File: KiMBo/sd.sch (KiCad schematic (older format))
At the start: 9 parts

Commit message: Annotate all components, now passing ERC, added ferrites to the rest of the connectors
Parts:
- gave numbers to parts that had none: 9
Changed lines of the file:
@@
 $Descr A4 11693 8268
 encoding utf-8
-Sheet 10 26
+Sheet 13 26
 Title ""
 Date ""
@@
 $EndDescr
 $Comp
-L CP1 C?
+L CP1 C65
 U 1 1 589C8DA1
 P 6900 2750
-F 0 "C?" H 7015 2796 50  0000 L CNN
+F 0 "C65" H 7015 2796 50  0000 L CNN
 F 1 "CP1" H 7015 2705 50  0000 L CNN
 F 2 "" H 6900 2750 50  0000 C CNN
@@
 $EndComp
 $Comp
-L CP1 C?
+L CP1 C66
 U 1 1 589C8DE9
 P 7100 2750
-F 0 "C?" H 7215 2796 50  0000 L CNN
+F 0 "C66" H 7215 2796 50  0000 L CNN
 F 1 "CP1" H 7215 2705 50  0000 L CNN
 F 2 "" H 7100 2750 50  0000 C CNN
@@
 Connection ~ 7000 2950
 $Comp
-L GND #PWR0166
+L GND #PWR0146
 U 1 1 589C8FE8
 P 7000 3000
-F 0 "#PWR0166" H 7000 2750 50  0001 C CNN
+F 0 "#PWR0146" H 7000 2750 50  0001 C CNN
 F 1 "GND" H 7005 2827 50  0000 C CNN
 F 2 "" H 7000 3000 50  0000 C CNN
@@
 	4800 3900 6600 3900
 $Comp
-L R R?
+L R R99
 U 1 1 58F3951D
 P 5300 3100
-F 0 "R?" H 5370 3146 50  0000 L CNN
+F 0 "R99" H 5370 3146 50  0000 L CNN
 F 1 "R" H 5370 3055 50  0000 L CNN
 F 2 "" V 5230 3100 50  0000 C CNN
@@
 $EndComp
 $Comp
-L R R?
+L R R100
 U 1 1 58F3959D
 P 5550 3100
-F 0 "R?" H 5620 3146 50  0000 L CNN
+F 0 "R100" H 5620 3146 50  0000 L CNN
 F 1 "R" H 5620 3055 50  0000 L CNN
 F 2 "" V 5480 3100 50  0000 C CNN
@@
 $EndComp
 $Comp
-L R R?
+L R R101
 U 1 1 58F395D9
 P 5800 3100
-F 0 "R?" H 5870 3146 50  0000 L CNN
+F 0 "R101" H 5870 3146 50  0000 L CNN
 F 1 "R" H 5870 3055 50  0000 L CNN
 F 2 "" V 5730 3100 50  0000 C CNN
@@
 $EndComp
 $Comp
-L R R?
+L R R102
 U 1 1 58F39A19
 P 6050 3100
-F 0 "R?" H 6120 3146 50  0000 L CNN
+F 0 "R102" H 6120 3146 50  0000 L CNN
 F 1 "R" H 6120 3055 50  0000 L CNN
 F 2 "" V 5980 3100 50  0000 C CNN
@@
 $EndComp
 $Comp
-L R R?
+L R R103
 U 1 1 58F39B2F
 P 6300 3100
-F 0 "R?" H 6370 3146 50  0000 L CNN
+F 0 "R103" H 6370 3146 50  0000 L CNN
 F 1 "R" H 6370 3055 50  0000 L CNN
 F 2 "" V 6230 3100 50  0000 C CNN
@@
 $EndComp
 $Comp
-L R R?
+L R R104
 U 1 1 58F39B72
 P 6550 3100
-F 0 "R?" H 6620 3146 50  0000 L CNN
+F 0 "R104" H 6620 3146 50  0000 L CNN
 F 1 "R" H 6620 3055 50  0000 L CNN
 F 2 "" V 6480 3100 50  0000 C CNN
@@
 SPI0_CS1
 $Comp
-L R R?
+L R R98
 U 1 1 58F3C883
 P 5050 3100
-F 0 "R?" H 5120 3146 50  0000 L CNN
+F 0 "R98" H 5120 3146 50  0000 L CNN
 F 1 "R" H 5120 3055 50  0000 L CNN
 F 2 "" V 4980 3100 50  0000 C CNN
@@
 G17
 $Comp
-L VDD_3V3B #PWR0167
+L VDD_3V3B #PWR0147
 U 1 1 5A066650
 P 5800 2850
-F 0 "#PWR0167" H 5800 2700 50  0001 C CNN
+F 0 "#PWR0147" H 5800 2700 50  0001 C CNN
 F 1 "VDD_3V3B" H 5815 3023 50  0000 C CNN
 F 2 "" H 5800 2850 50  0000 C CNN
@@
 $EndComp
 $Comp
-L VDD_3V3B #PWR0168
+L VDD_3V3B #PWR0148
 U 1 1 5A066680
 P 7000 2500
-F 0 "#PWR0168" H 7000 2350 50  0001 C CNN
+F 0 "#PWR0148" H 7000 2350 50  0001 C CNN
 F 1 "VDD_3V3B" H 7015 2673 50  0000 C CNN
 F 2 "" H 7000 2500 50  0000 C CNN

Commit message: Clean up various parts of the schematic, high level sheet has annoated modules
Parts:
- renumbered C65 to C42, C66 to C43, R98 to R86, R99 to R87, R100 to R88, R101 to R89, R102 to R90, R103 to R91, R104 to R92
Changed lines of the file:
@@
 $Descr A4 11693 8268
 encoding utf-8
-Sheet 13 26
+Sheet 9 26
 Title ""
 Date ""
@@
 $EndDescr
 $Comp
-L CP1 C65
+L CP1 C42
 U 1 1 589C8DA1
 P 6900 2750
-F 0 "C65" H 7015 2796 50  0000 L CNN
+F 0 "C42" H 7015 2796 50  0000 L CNN
 F 1 "CP1" H 7015 2705 50  0000 L CNN
 F 2 "" H 6900 2750 50  0000 C CNN
@@
 $EndComp
 $Comp
-L CP1 C66
+L CP1 C43
 U 1 1 589C8DE9
 P 7100 2750
-F 0 "C66" H 7215 2796 50  0000 L CNN
+F 0 "C43" H 7215 2796 50  0000 L CNN
 F 1 "CP1" H 7215 2705 50  0000 L CNN
 F 2 "" H 7100 2750 50  0000 C CNN
@@
 	4800 3900 6600 3900
 $Comp
-L R R99
+L R R87
 U 1 1 58F3951D
 P 5300 3100
-F 0 "R99" H 5370 3146 50  0000 L CNN
+F 0 "R87" H 5370 3146 50  0000 L CNN
 F 1 "R" H 5370 3055 50  0000 L CNN
 F 2 "" V 5230 3100 50  0000 C CNN
@@
 $EndComp
 $Comp
-L R R100
+L R R88
 U 1 1 58F3959D
 P 5550 3100
-F 0 "R100" H 5620 3146 50  0000 L CNN
+F 0 "R88" H 5620 3146 50  0000 L CNN
 F 1 "R" H 5620 3055 50  0000 L CNN
 F 2 "" V 5480 3100 50  0000 C CNN
@@
 $EndComp
 $Comp
-L R R101
+L R R89
 U 1 1 58F395D9
 P 5800 3100
-F 0 "R101" H 5870 3146 50  0000 L CNN
+F 0 "R89" H 5870 3146 50  0000 L CNN
 F 1 "R" H 5870 3055 50  0000 L CNN
 F 2 "" V 5730 3100 50  0000 C CNN
@@
 $EndComp
 $Comp
-L R R102
+L R R90
 U 1 1 58F39A19
 P 6050 3100
-F 0 "R102" H 6120 3146 50  0000 L CNN
+F 0 "R90" H 6120 3146 50  0000 L CNN
 F 1 "R" H 6120 3055 50  0000 L CNN
 F 2 "" V 5980 3100 50  0000 C CNN
@@
 $EndComp
 $Comp
-L R R103
+L R R91
 U 1 1 58F39B2F
 P 6300 3100
-F 0 "R103" H 6370 3146 50  0000 L CNN
+F 0 "R91" H 6370 3146 50  0000 L CNN
 F 1 "R" H 6370 3055 50  0000 L CNN
 F 2 "" V 6230 3100 50  0000 C CNN
@@
 $EndComp
 $Comp
-L R R104
+L R R92
 U 1 1 58F39B72
 P 6550 3100
-F 0 "R104" H 6620 3146 50  0000 L CNN
+F 0 "R92" H 6620 3146 50  0000 L CNN
 F 1 "R" H 6620 3055 50  0000 L CNN
 F 2 "" V 6480 3100 50  0000 C CNN
@@
 SPI0_CS1
 $Comp
-L R R98
+L R R86
 U 1 1 58F3C883
 P 5050 3100
-F 0 "R98" H 5120 3146 50  0000 L CNN
+F 0 "R86" H 5120 3146 50  0000 L CNN
 F 1 "R" H 5120 3055 50  0000 L CNN
 F 2 "" V 4980 3100 50  0000 C CNN

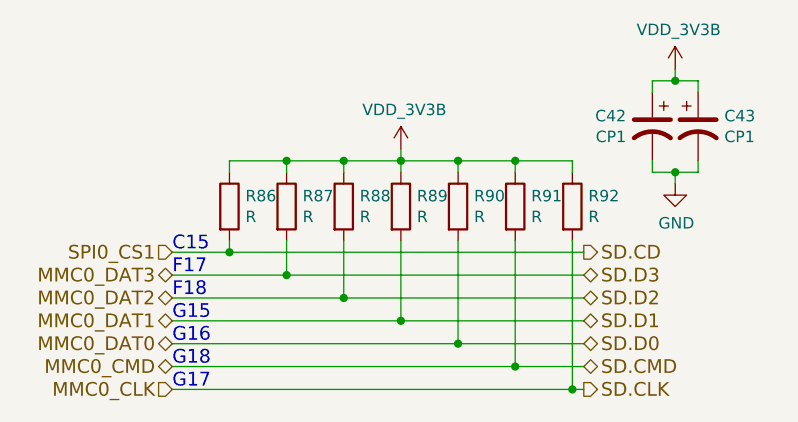
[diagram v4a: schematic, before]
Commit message: Entry of additional component values
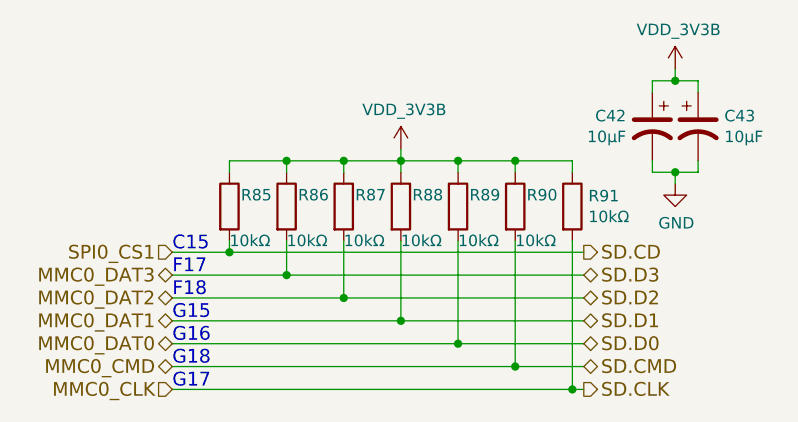
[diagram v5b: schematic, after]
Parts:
- C42, C43: value CP1 -> 10μF
- R85: renamed from R86; value R -> 10kΩ
- R86: renamed from R87; value R -> 10kΩ
- R87: renamed from R88; value R -> 10kΩ
- R88: renamed from R89; value R -> 10kΩ
- R89: renamed from R90; value R -> 10kΩ
- R90: renamed from R91; value R -> 10kΩ
- R91: renamed from R92; value R -> 10kΩ
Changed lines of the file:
@@
 P 6900 2750
 F 0 "C42" H 7015 2796 50  0000 L CNN
-F 1 "CP1" H 7015 2705 50  0000 L CNN
+F 1 "10μF" H 7015 2705 50  0000 L CNN
 F 2 "" H 6900 2750 50  0001 C CNN
 F 3 "" H 6900 2750 50  0000 C CNN
@@
 P 7100 2750
 F 0 "C43" H 7215 2796 50  0000 L CNN
-F 1 "CP1" H 7215 2705 50  0000 L CNN
+F 1 "10μF" H 7215 2705 50  0000 L CNN
 F 2 "" H 7100 2750 50  0001 C CNN
 F 3 "" H 7100 2750 50  0000 C CNN
@@
 Connection ~ 7000 2950
 $Comp
-L GND #PWR0146
+L GND #PWR0147
 U 1 1 589C8FE8
 P 7000 3000
-F 0 "#PWR0146" H 7000 2750 50  0001 C CNN
+F 0 "#PWR0147" H 7000 2750 50  0001 C CNN
 F 1 "GND" H 7005 2827 50  0000 C CNN
 F 2 "" H 7000 3000 50  0000 C CNN
@@
 	4800 3900 6600 3900
 $Comp
-L R R87
+L R R86
 U 1 1 58F3951D
 P 5300 3100
-F 0 "R87" H 5370 3146 50  0000 L CNN
-F 1 "R" H 5370 3055 50  0000 L CNN
+F 0 "R86" H 5350 3150 50  0000 L CNN
+F 1 "10kΩ" H 5300 2950 50  0000 L CNN
 F 2 "" V 5230 3100 50  0001 C CNN
 F 3 "" H 5300 3100 50  0000 C CNN
@@
 $EndComp
 $Comp
-L R R88
+L R R87
 U 1 1 58F3959D
 P 5550 3100
-F 0 "R88" H 5620 3146 50  0000 L CNN
-F 1 "R" H 5620 3055 50  0000 L CNN
+F 0 "R87" H 5600 3150 50  0000 L CNN
+F 1 "10kΩ" H 5550 2950 50  0000 L CNN
 F 2 "" V 5480 3100 50  0001 C CNN
 F 3 "" H 5550 3100 50  0000 C CNN
@@
 $EndComp
 $Comp
-L R R89
+L R R88
 U 1 1 58F395D9
 P 5800 3100
-F 0 "R89" H 5870 3146 50  0000 L CNN
-F 1 "R" H 5870 3055 50  0000 L CNN
+F 0 "R88" H 5850 3150 50  0000 L CNN
+F 1 "10kΩ" H 5800 2950 50  0000 L CNN
 F 2 "" V 5730 3100 50  0001 C CNN
 F 3 "" H 5800 3100 50  0000 C CNN
@@
 $EndComp
 $Comp
-L R R90
+L R R89
 U 1 1 58F39A19
 P 6050 3100
-F 0 "R90" H 6120 3146 50  0000 L CNN
-F 1 "R" H 6120 3055 50  0000 L CNN
+F 0 "R89" H 6100 3150 50  0000 L CNN
+F 1 "10kΩ" H 6050 2950 50  0000 L CNN
 F 2 "" V 5980 3100 50  0001 C CNN
 F 3 "" H 6050 3100 50  0000 C CNN
@@
 $EndComp
 $Comp
-L R R91
+L R R90
 U 1 1 58F39B2F
 P 6300 3100
-F 0 "R91" H 6370 3146 50  0000 L CNN
-F 1 "R" H 6370 3055 50  0000 L CNN
+F 0 "R90" H 6350 3150 50  0000 L CNN
+F 1 "10kΩ" H 6300 2950 50  0000 L CNN
 F 2 "" V 6230 3100 50  0001 C CNN
 F 3 "" H 6300 3100 50  0000 C CNN
@@
 $EndComp
 $Comp
-L R R92
+L R R91
 U 1 1 58F39B72
 P 6550 3100
-F 0 "R92" H 6620 3146 50  0000 L CNN
-F 1 "R" H 6620 3055 50  0000 L CNN
+F 0 "R91" H 6620 3146 50  0000 L CNN
+F 1 "10kΩ" H 6620 3055 50  0000 L CNN
 F 2 "" V 6480 3100 50  0001 C CNN
 F 3 "" H 6550 3100 50  0000 C CNN
@@
 SPI0_CS1
 $Comp
-L R R86
+L R R85
 U 1 1 58F3C883
 P 5050 3100
-F 0 "R86" H 5120 3146 50  0000 L CNN
-F 1 "R" H 5120 3055 50  0000 L CNN
+F 0 "R85" H 5100 3150 50  0000 L CNN
+F 1 "10kΩ" H 5050 2950 50  0000 L CNN
 F 2 "" V 4980 3100 50  0001 C CNN
 F 3 "" H 5050 3100 50  0000 C CNN
@@
 G17
 $Comp
-L VDD_3V3B #PWR0147
+L VDD_3V3B #PWR0148
 U 1 1 5A066650
 P 5800 2850
-F 0 "#PWR0147" H 5800 2700 50  0001 C CNN
+F 0 "#PWR0148" H 5800 2700 50  0001 C CNN
 F 1 "VDD_3V3B" H 5815 3023 50  0000 C CNN
 F 2 "" H 5800 2850 50  0000 C CNN
@@
 $EndComp
 $Comp
-L VDD_3V3B #PWR0148
+L VDD_3V3B #PWR0149
 U 1 1 5A066680
 P 7000 2500
-F 0 "#PWR0148" H 7000 2350 50  0001 C CNN
+F 0 "#PWR0149" H 7000 2350 50  0001 C CNN
 F 1 "VDD_3V3B" H 7015 2673 50  0000 C CNN
 F 2 "" H 7000 2500 50  0000 C CNN

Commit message: Replace most electrolytic cap symbols symbols with the standard, non-polarized (ceramic) cap symbol
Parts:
- C42, C43: symbol CP1 -> C
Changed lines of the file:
@@
 $EndDescr
 $Comp
-L CP1 C42
+L C C42
 U 1 1 589C8DA1
 P 6900 2750
@@
 $EndComp
 $Comp
-L CP1 C43
+L C C43
 U 1 1 589C8DE9
 P 7100 2750

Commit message: Associate more footprints
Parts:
- C42, C43: footprint (none) -> Capacitors_SMD:C_0603
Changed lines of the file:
@@
 F 0 "C42" H 7015 2796 50  0000 L CNN
 F 1 "10μF" H 7015 2705 50  0000 L CNN
-F 2 "" H 6900 2750 50  0001 C CNN
+F 2 "Capacitors_SMD:C_0603" H 6900 2750 50  0001 C CNN
 F 3 "" H 6900 2750 50  0000 C CNN
 	1    6900 2750
@@
 F 0 "C43" H 7215 2796 50  0000 L CNN
 F 1 "10μF" H 7215 2705 50  0000 L CNN
-F 2 "" H 7100 2750 50  0001 C CNN
+F 2 "Capacitors_SMD:C_0603" H 7100 2750 50  0001 C CNN
 F 3 "" H 7100 2750 50  0000 C CNN
 	1    7100 2750

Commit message: Add equivalent annotations document, associate more footprints
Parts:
- R84: renamed from R85; footprint (none) -> Resistors_SMD:R_0402
- R85: renamed from R86; footprint (none) -> Resistors_SMD:R_0402
- R86: renamed from R87; footprint (none) -> Resistors_SMD:R_0402
- R87: renamed from R88; footprint (none) -> Resistors_SMD:R_0402
- R88: renamed from R89; footprint (none) -> Resistors_SMD:R_0402
- R89: renamed from R90; footprint (none) -> Resistors_SMD:R_0402
- R90: renamed from R91; footprint (none) -> Resistors_SMD:R_0402
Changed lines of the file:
@@
 Connection ~ 7000 2950
 $Comp
-L GND #PWR0147
+L GND #PWR0146
 U 1 1 589C8FE8
 P 7000 3000
-F 0 "#PWR0147" H 7000 2750 50  0001 C CNN
+F 0 "#PWR0146" H 7000 2750 50  0001 C CNN
 F 1 "GND" H 7005 2827 50  0000 C CNN
 F 2 "" H 7000 3000 50  0000 C CNN
@@
 	4800 3900 6600 3900
 $Comp
-L R R86
+L R R85
 U 1 1 58F3951D
 P 5300 3100
-F 0 "R86" H 5350 3150 50  0000 L CNN
+F 0 "R85" H 5350 3150 50  0000 L CNN
 F 1 "10kΩ" H 5300 2950 50  0000 L CNN
-F 2 "" V 5230 3100 50  0001 C CNN
+F 2 "Resistors_SMD:R_0402" V 5230 3100 50  0001 C CNN
 F 3 "" H 5300 3100 50  0000 C CNN
 	1    5300 3100
@@
 $EndComp
 $Comp
-L R R87
+L R R86
 U 1 1 58F3959D
 P 5550 3100
-F 0 "R87" H 5600 3150 50  0000 L CNN
+F 0 "R86" H 5600 3150 50  0000 L CNN
 F 1 "10kΩ" H 5550 2950 50  0000 L CNN
-F 2 "" V 5480 3100 50  0001 C CNN
+F 2 "Resistors_SMD:R_0402" V 5480 3100 50  0001 C CNN
 F 3 "" H 5550 3100 50  0000 C CNN
 	1    5550 3100
@@
 $EndComp
 $Comp
-L R R88
+L R R87
 U 1 1 58F395D9
 P 5800 3100
-F 0 "R88" H 5850 3150 50  0000 L CNN
+F 0 "R87" H 5850 3150 50  0000 L CNN
 F 1 "10kΩ" H 5800 2950 50  0000 L CNN
-F 2 "" V 5730 3100 50  0001 C CNN
+F 2 "Resistors_SMD:R_0402" V 5730 3100 50  0001 C CNN
 F 3 "" H 5800 3100 50  0000 C CNN
 	1    5800 3100
@@
 $EndComp
 $Comp
-L R R89
+L R R88
 U 1 1 58F39A19
 P 6050 3100
-F 0 "R89" H 6100 3150 50  0000 L CNN
+F 0 "R88" H 6100 3150 50  0000 L CNN
 F 1 "10kΩ" H 6050 2950 50  0000 L CNN
-F 2 "" V 5980 3100 50  0001 C CNN
+F 2 "Resistors_SMD:R_0402" V 5980 3100 50  0001 C CNN
 F 3 "" H 6050 3100 50  0000 C CNN
 	1    6050 3100
@@
 $EndComp
 $Comp
-L R R90
+L R R89
 U 1 1 58F39B2F
 P 6300 3100
-F 0 "R90" H 6350 3150 50  0000 L CNN
+F 0 "R89" H 6350 3150 50  0000 L CNN
 F 1 "10kΩ" H 6300 2950 50  0000 L CNN
-F 2 "" V 6230 3100 50  0001 C CNN
+F 2 "Resistors_SMD:R_0402" V 6230 3100 50  0001 C CNN
 F 3 "" H 6300 3100 50  0000 C CNN
 	1    6300 3100
@@
 $EndComp
 $Comp
-L R R91
+L R R90
 U 1 1 58F39B72
 P 6550 3100
-F 0 "R91" H 6620 3146 50  0000 L CNN
+F 0 "R90" H 6620 3146 50  0000 L CNN
 F 1 "10kΩ" H 6620 3055 50  0000 L CNN
-F 2 "" V 6480 3100 50  0001 C CNN
+F 2 "Resistors_SMD:R_0402" V 6480 3100 50  0001 C CNN
 F 3 "" H 6550 3100 50  0000 C CNN
 	1    6550 3100
@@
 SPI0_CS1
 $Comp
-L R R85
+L R R84
 U 1 1 58F3C883
 P 5050 3100
-F 0 "R85" H 5100 3150 50  0000 L CNN
+F 0 "R84" H 5100 3150 50  0000 L CNN
 F 1 "10kΩ" H 5050 2950 50  0000 L CNN
-F 2 "" V 4980 3100 50  0001 C CNN
+F 2 "Resistors_SMD:R_0402" V 4980 3100 50  0001 C CNN
 F 3 "" H 5050 3100 50  0000 C CNN
 	1    5050 3100
@@
 G17
 $Comp
-L VDD_3V3B #PWR0148
+L VDD_3V3B #PWR0147
 U 1 1 5A066650
 P 5800 2850
-F 0 "#PWR0148" H 5800 2700 50  0001 C CNN
+F 0 "#PWR0147" H 5800 2700 50  0001 C CNN
 F 1 "VDD_3V3B" H 5815 3023 50  0000 C CNN
 F 2 "" H 5800 2850 50  0000 C CNN
@@
 $EndComp
 $Comp
-L VDD_3V3B #PWR0149
+L VDD_3V3B #PWR0148
 U 1 1 5A066680
 P 7000 2500
-F 0 "#PWR0149" H 7000 2350 50  0001 C CNN
+F 0 "#PWR0148" H 7000 2350 50  0001 C CNN
 F 1 "VDD_3V3B" H 7015 2673 50  0000 C CNN
 F 2 "" H 7000 2500 50  0000 C CNN
